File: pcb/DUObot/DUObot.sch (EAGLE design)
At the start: 1 part

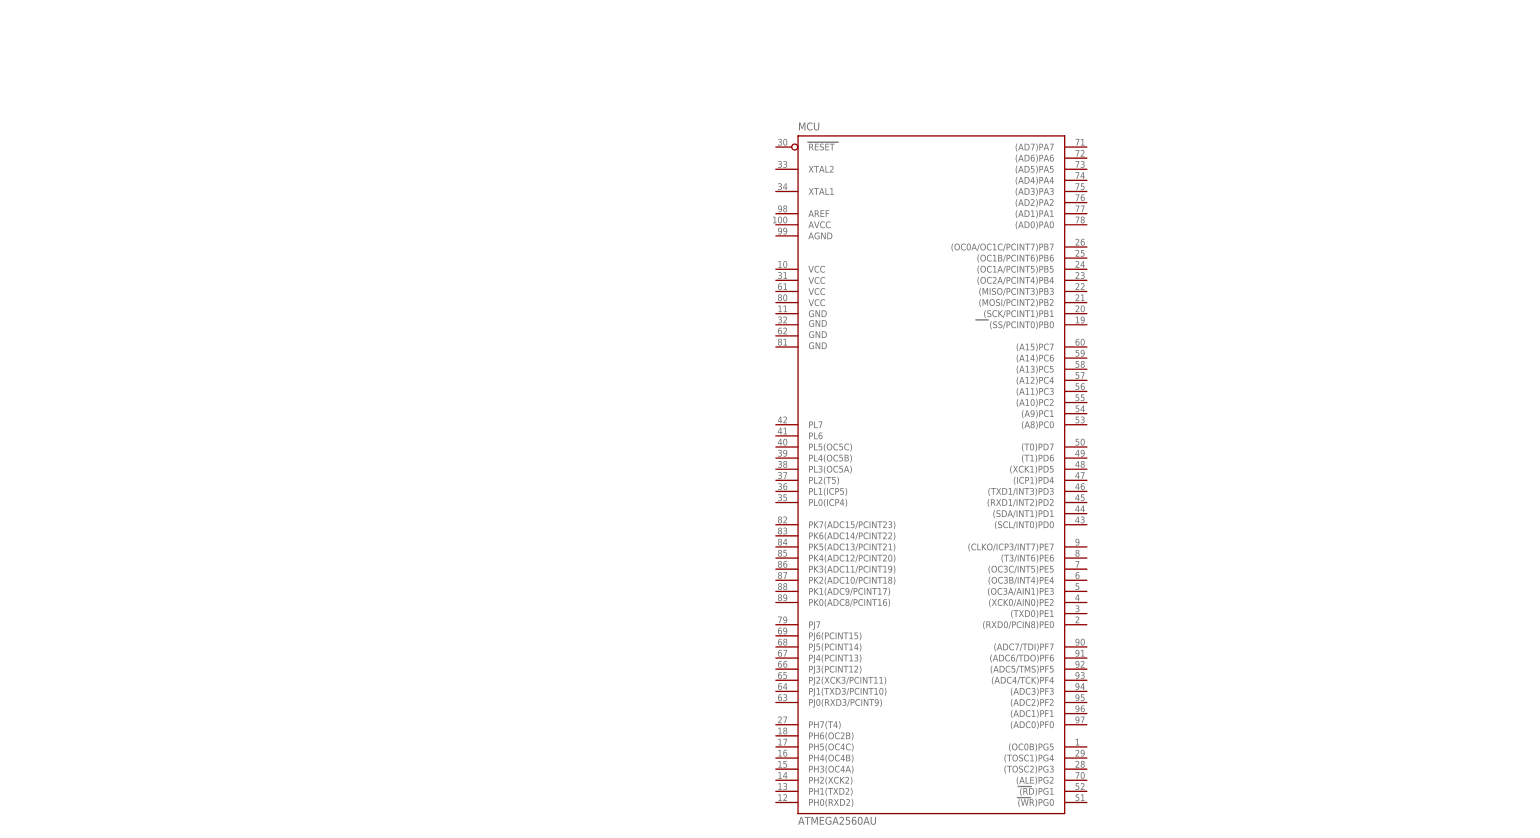
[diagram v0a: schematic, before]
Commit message: Add more components to main board. Start pcb layout
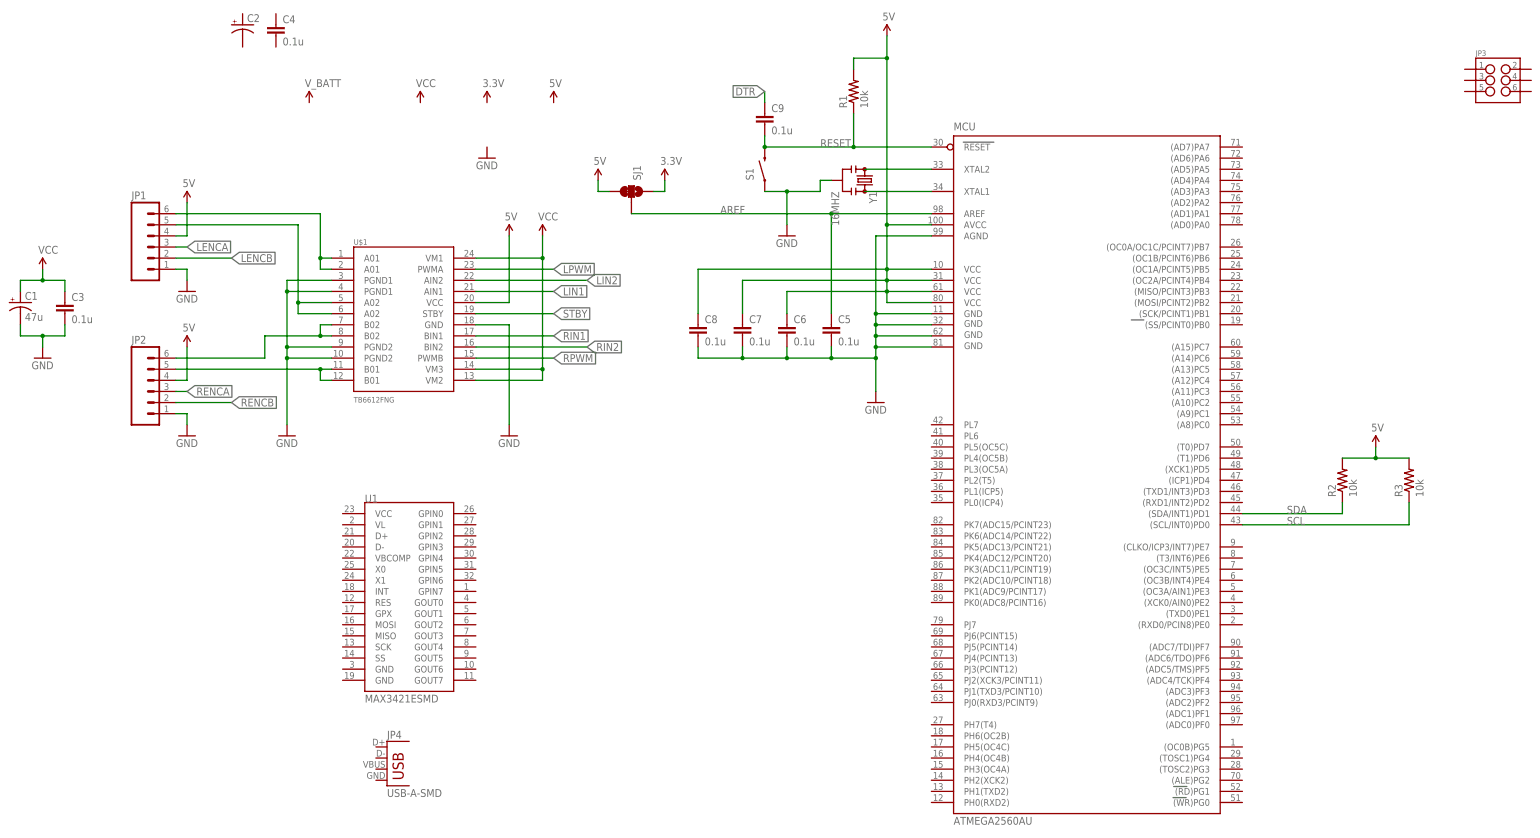
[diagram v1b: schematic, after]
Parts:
- added C1: 47u, SparkFun-Capacitors:CAP_POLD
- added C2: (no value), SparkFun-Capacitors:CAP_POLD
- added C3, C4, C5, C6, C7, C8, C9: 0.1u, SparkFun-Passives:CAP0805
- added JP1, JP2: (no value), SparkFun-Connectors:M06SMD-1MM
- added JP3: (no value), SparkFun-Connectors:M03X2SMT
- added JP4: USB-A-SMD, SparkFun-Connectors:USB-A-SMD
- added R1, R2, R3: 10k, SparkFun-Passives:RESISTOR0805-RES
- added S1: SWITCH-MOMENTARY-2SMD-4, SparkFun-Electromechanical:SWITCH-MOMENTARY-2SMD-4
- added SJ1: JUMPER-PAD-3-2OF3_NC_BY_TRACE_SMALL, SparkFun-Passives:JUMPER-PAD-3-2OF3_NC_BY_TRACE_SMALL
- added U$1: TB6612FNG, SparkFun-PowerIC:TB6612FNG
- added U1: MAX3421ESMD, SparkFun-DigitalIC:MAX3421ESMD
- added Y1: 16MHZ, SparkFun-FreqCtrl:RESONATOR16MHZ
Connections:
- new net 3.3V: SJ1.1
- new net 5V: C6.1, C7.1, C8.1, JP1.4, JP2.4, MCU.AVCC, MCU.VCC, MCU.VCC1, MCU.VCC2, MCU.VCC3, R1.2, R2.2, R3.2, SJ1.3, U$1.VCC
- new net AREF: C5.1, MCU.AREF, SJ1.2
- new net DTR: C9.1
- new net GND: C1.-, C3.2, C5.2, C6.2, C7.2, C8.2, JP1.1, JP2.1, MCU.AGND, MCU.GND, MCU.GND1, MCU.GND2, MCU.GND3, S1.1, U$1.GND, U$1.PGND1@3, U$1.PGND1@4, U$1.PGND2@10, U$1.PGND2@9, Y1.2
- new net LENCA: JP1.3
- new net LENCB: JP1.2
- new net LIN1: U$1.AIN1
- new net LIN2: U$1.AIN2
- new net LPWM: U$1.PWMA
- new net N$1: JP2.5, U$1.B01@11, U$1.B01@12
- new net N$2: JP2.6, U$1.B02@7, U$1.B02@8
- new net N$3: JP1.6, U$1.A01@1, U$1.A01@2
- new net N$4: JP1.5, U$1.A02@5, U$1.A02@6
- new net N$5: MCU.XTAL2, Y1.1
- new net N$6: MCU.XTAL1, Y1.3
- new net RENCA: JP2.3
- new net RENCB: JP2.2
- new net RESET: C9.2, MCU.RESET, R1.1, S1.2
- new net RIN1: U$1.BIN1
- new net RIN2: U$1.BIN2
- new net RPWM: U$1.PWMB
- new net SCL: MCU.(SCL/INT0)PD0, R3.1
- new net SDA: MCU.(SDA/INT1)PD1, R2.1
- new net STBY: U$1.STBY
- new net VCC: C1.+, C3.1, U$1.VM1, U$1.VM2, U$1.VM3
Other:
- moved on the sheet: MCU

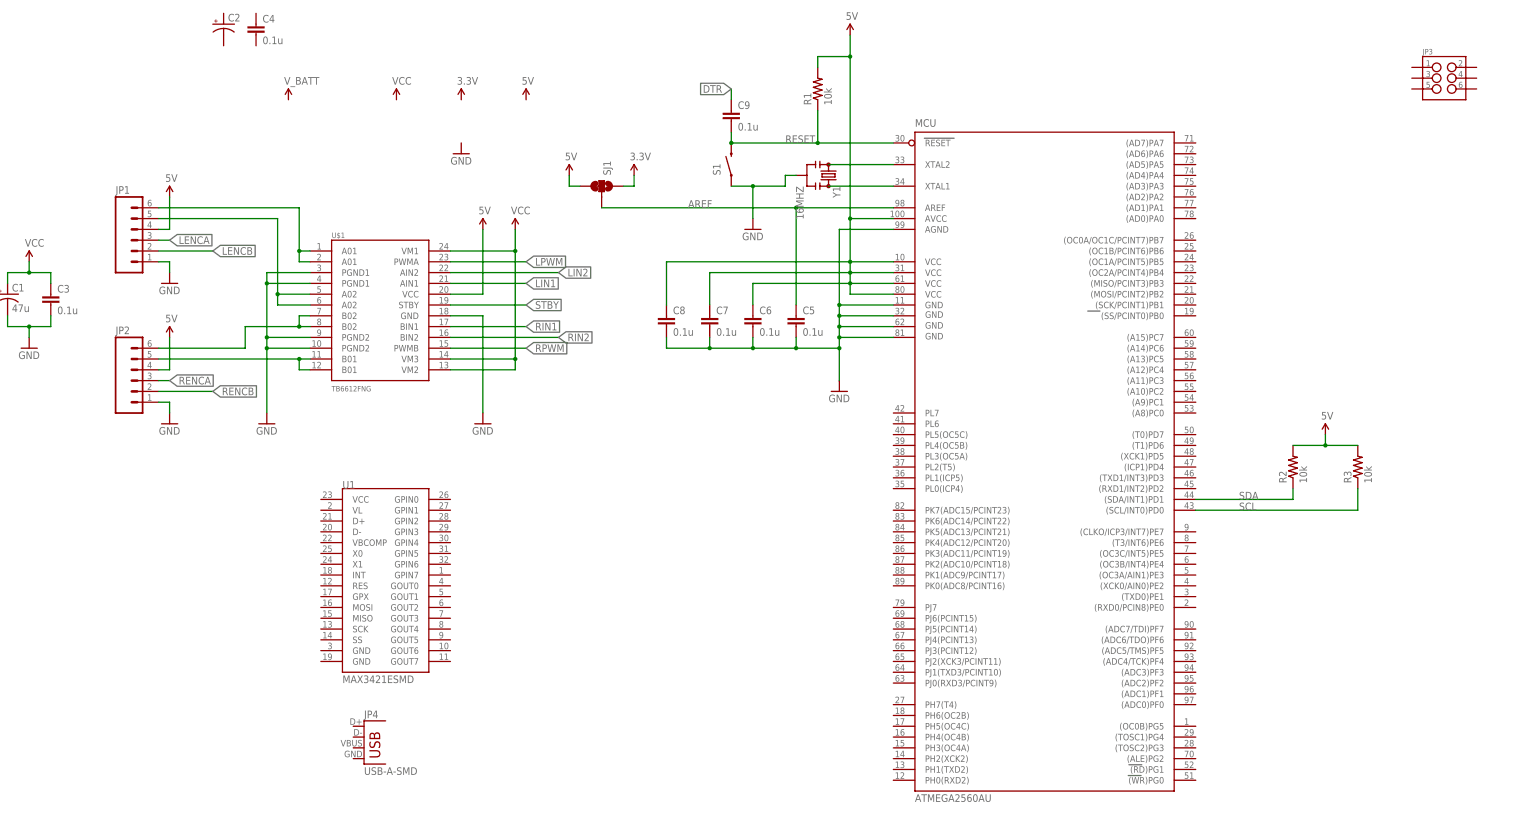
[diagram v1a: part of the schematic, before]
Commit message: Continue adding components to schematic
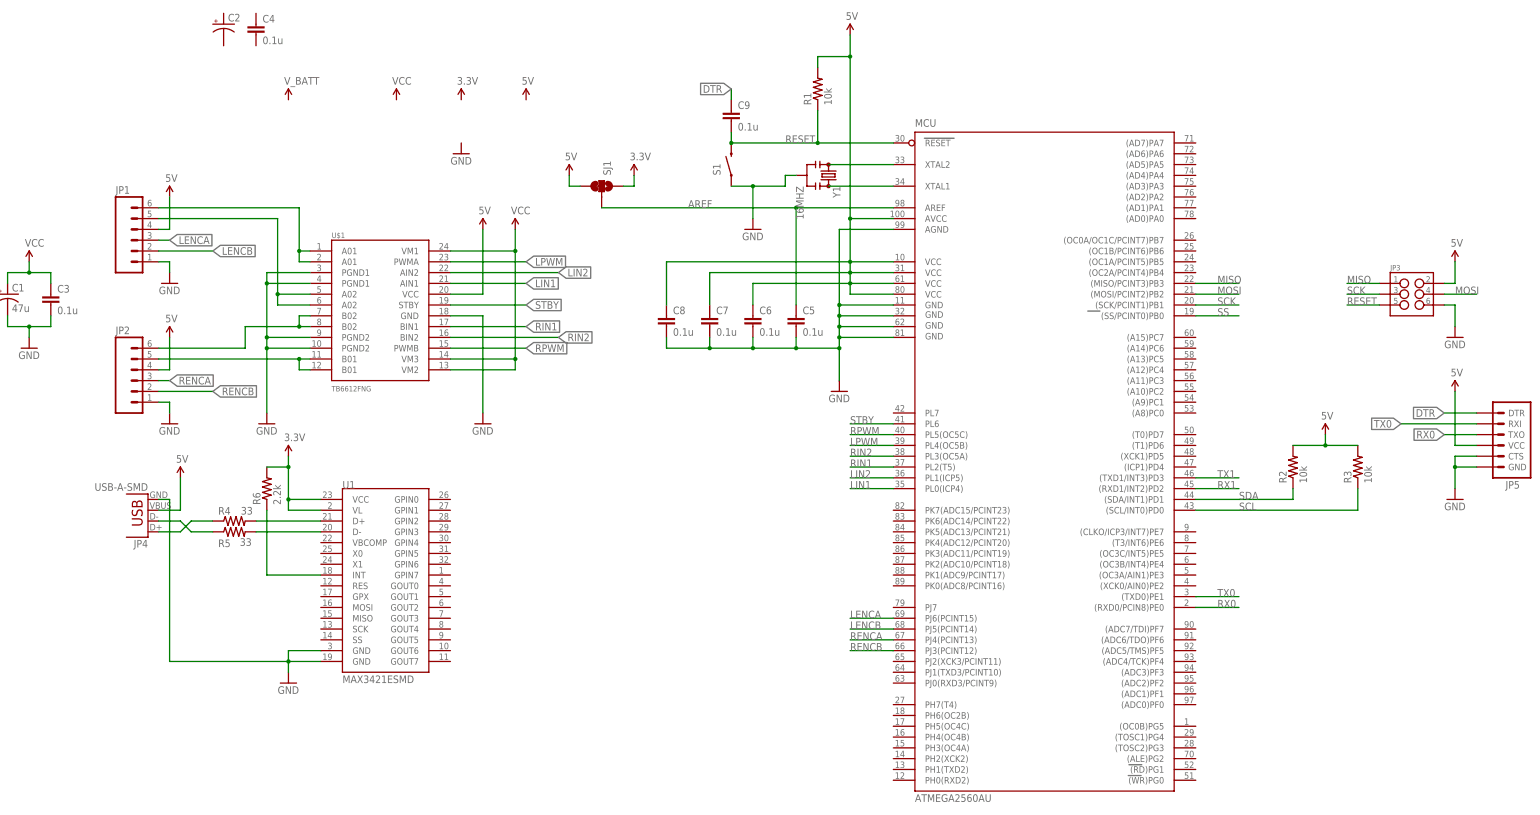
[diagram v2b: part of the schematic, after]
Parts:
- added JP5: (no value), SparkFun-Connectors:ARDUINO_SERIAL_PROGRAMPTH
- added R4, R5: 33, SparkFun-Passives:RESISTOR0805-RES
- added R6: 2.2k, SparkFun-Passives:RESISTOR0805-RES
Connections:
- new net MISO: JP3.1, MCU.(MISO/PCINT3)PB3
- new net MOSI: JP3.4, MCU.(MOSI/PCINT2)PB2
- new net N$10: JP4.D-, R5.1
- new net N$11: R6.1, U1.INT
- new net N$7: JP4.D+, R4.1
- new net N$8: R5.2, U1.D-
- new net N$9: R4.2, U1.D+
- new net RX0: JP5.TXO, MCU.(RXD0/PCIN8)PE0
- new net RX1: MCU.(RXD1/INT2)PD2
- new net SCK: JP3.3, MCU.(SCK/PCINT1)PB1
- new net SS: MCU.(SS/PCINT0)PB0
- new net TX0: JP5.RXI, MCU.(TXD0)PE1
- new net TX1: MCU.(TXD1/INT3)PD3
- net 3.3V: now also R6.2, U1.VCC, U1.VL
- net 5V: now also JP3.2, JP4.VBUS, JP5.VCC
- net DTR: now also JP5.DTR
- net GND: now also JP3.6, JP4.GND, JP5.CTS, JP5.GND, U1.GND@19, U1.GND@3
- net LENCA: now also MCU.PJ6(PCINT15)
- net LENCB: now also MCU.PJ5(PCINT14)
- net LIN1: now also MCU.PL0(ICP4)
- net LIN2: now also MCU.PL1(ICP5)
- net LPWM: now also MCU.PL4(OC5B)
- net RENCA: now also MCU.PJ4(PCINT13)
- net RENCB: now also MCU.PJ3(PCINT12)
- net RESET: now also JP3.5
- net RIN1: now also MCU.PL2(T5)
- net RIN2: now also MCU.PL3(OC5A)
- net RPWM: now also MCU.PL5(OC5C)
- net STBY: now also MCU.PL6
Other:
- moved on the sheet: JP3, JP4

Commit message: Working on power select control circuitry
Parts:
- added C10: 0.1u, SparkFun-Passives:CAP0805
- added JP6: (no value), SparkFun-Connectors:M05SMD2
- added R7: 1M, SparkFun-Passives:RESISTOR0805-RES
- JP3: value (none) -> AVR_SPI_PRG_6TESTPOINTS; device SparkFun-Connectors:M03X2SMT -> SparkFun-Connectors:AVR_SPI_PRG_6TESTPOINTS
- SJ1: value JUMPER-PAD-3-2OF3_NC_BY_TRACE_SMALL -> JUMPER-PAD-3-NOYES_SILK; device SparkFun-Passives:JUMPER-PAD-3-2OF3_NC_BY_TRACE_SMALL -> SparkFun-Passives:JUMPER-PAD-3-NOYES_SILK
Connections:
- net 3.3V: now also JP6.2
- net 5V: now also C10.1, JP6.1
- net GND: now also C10.2, JP6.3, S1.2; no longer S1.1
- net N$5: now also R7.2
- net N$6: now also R7.1
- net RESET: now also S1.1; no longer S1.2
- net SCL: now also JP6.5
- net SDA: now also JP6.4
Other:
- moved on the sheet: C1, C3, C9, JP1, JP2, R1, S1, U$1, Y1

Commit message: Main board mostly finished - needs minor changes/additions
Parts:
- removed JP1, JP2: (no value), SparkFun-Connectors:M06SMD-1MM
- removed JP3: AVR_SPI_PRG_6TESTPOINTS, SparkFun-Connectors:AVR_SPI_PRG_6TESTPOINTS
- removed JP4: USB-A-SMD, SparkFun-Connectors:USB-A-SMD
- removed JP5: (no value), SparkFun-Connectors:ARDUINO_SERIAL_PROGRAMPTH
- removed JP6: (no value), SparkFun-Connectors:M05SMD2
- added 3V3_PWR, 5V_PWR: (no value), SparkFun-LED:LED0805
- added C11, C12, C13, C15, C17: 0.1u, SparkFun-Passives:CAP0805
- added C14, C16: 10u, SparkFun-Passives:CAP_POL1206
- added C18, C19: 470p, SparkFun-Passives:CAP0805
- added D1: B340A, SparkFun-DiscreteSemi:DIODE-SCHOTTKY-B340A
- added FTDI: (no value), SparkFun-Connectors:ARDUINO_SERIAL_PROGRAMPTH
- added ICSP: AVR_SPI_PRG_6TESTPOINTS, SparkFun-Connectors:AVR_SPI_PRG_6TESTPOINTS
- added IMU: (no value), SparkFun-Connectors:M05SMD2
- added LEFT_MOTOR, RIGHT_MOTOR: (no value), SparkFun-Connectors:M06SMD-1MM
- added POWER: (no value), SparkFun-Electromechanical:SWITCH-SPDT-SMD-A
- added Q1, Q2: 200mA/50V, SparkFun-DiscreteSemi:MOSFET-NCHANNELBSS138
- added R10, R12, R13, R8, R9: (no value), SparkFun-Passives:RESISTOR0805-RES
- added R11, R14, R15, R17: 10k, SparkFun-Passives:RESISTOR0805-RES
- added R16, R18, R19: 20k, SparkFun-Passives:RESISTOR0805-RES
- added S2: SWITCH-MOMENTARY-2SMD-4, SparkFun-Electromechanical:SWITCH-MOMENTARY-2SMD-4
- added SG1: BUZZERPTH-KIT, SparkFun-Electromechanical:BUZZERPTH-KIT
- added U$2: 74AHC1G08, SparkFun-DigitalIC:74AHC1G08
- added U$3: LED-TRICOLOR, SparkFun-LED:LED-TRICOLOR
- added U$4: MCP6021T-E/OT, SparkFun-AnalogIC:MCP6021T-E/OT
- added U2: MIC5219 5V, SparkFun-PowerIC:V_REG_MIC52195V
- added U3: 3.3V/150mA, SparkFun-PowerIC:V_REG_MIC52053.3V
- added USB: USB-A-SMD, SparkFun-Connectors:USB-A-SMD
- added Y2: 12MHZ, SparkFun-FreqCtrl:RESONATOR16MHZ
- C2: value (none) -> 47u
- SJ1: value JUMPER-PAD-3-NOYES_SILK -> JUMPER-PAD-2-NOYES_SILK; device SparkFun-Passives:JUMPER-PAD-3-NOYES_SILK -> SparkFun-Passives:JUMPER-PAD-2-NOYES_SILK
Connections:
- net N$11 renamed U_INT
- new net BATT_LVL: MCU.PK7(ADC15/PCINT23), R16.1, R17.2
- new net BUZZER: MCU.(OC0B)PG5, Q1.G
- new net B_LED: MCU.(OC3A/AIN1)PE3, R9.1
- new net GPIO1: MCU.PK0(ADC8/PCINT16)
- new net GPIO2: MCU.PK1(ADC9/PCINT17)
- new net GPIO3: MCU.PK2(ADC10/PCINT18)
- new net GPIO4: MCU.PK3(ADC11/PCINT19)
- new net GPIO5: MCU.PK4(ADC12/PCINT20)
- new net GPIO6: MCU.PK5(ADC13/PCINT21)
- new net GPIO7: MCU.PK6(ADC14/PCINT22)
- new net G_LED: MCU.(OC3B/INT4)PE4, R10.1
- new net INT6: MCU.(T3/INT6)PE6
- new net INT7: MCU.(CLKO/ICP3/INT7)PE7, R11.1, S2.2
- new net N$11: R14.1, R15.2, U$4.+IN
- new net N$12: U$1.STBY, U$2.Y
- new net N$13: Q1.D, SG1.2
- new net N$14: R9.2, U$3.BLU
- new net N$15: R8.2, U$3.RED
- new net N$16: R10.2, U$3.GRN
- new net N$17: 5V_PWR.A, R12.1
- new net N$18: 3V3_PWR.A, R13.1
- new net N$19: U1.X0, Y2.1
- new net N$20: U1.X1, Y2.3
- new net N$21: C19.1, U2.BP
- new net N$22: C18.1, U3.BP
- new net N$23: U$4.V-
- new net N$24: U$4.V+
- new net N$25: D1.C, Q2.D
- new net N$27: POWER.O, R19.2
- new net N$28: POWER.S, R18.1
- new net N$29: POWER.P, Q2.G
- new net PWM1: MCU.PH3(OC4A)
- new net PWM2: MCU.PH4(OC4B)
- new net PWM3: MCU.PH5(OC4C)
- new net R_LED: MCU.(OC3C/INT5)PE5, R8.1
- new net U_MISO: U1.MISO
- new net U_MOSI: U1.MOSI
- new net U_RES: U1.RES
- new net U_SCK: U1.SCK
- new net U_SS: U1.SS
- new net V_BATT: D1.A, R18.2
- new net V_COMP: U$2.A, U$4.OUT
- net 3.3V: now also C11.1, C12.1, C14.+, C17.1, IMU.2, R13.2, SJ1.2, U$4.-IN, U3.OUT; no longer JP6.2, SJ1.1
- net 5V: now also C13.1, C15.1, C16.+, FTDI.VCC, ICSP.2, IMU.1, LEFT_MOTOR.4, R11.2, R12.2, RIGHT_MOTOR.4, SG1.1, U$2.VCC, U$3.A, U2.OUT, U3.EN, U3.IN, USB.VBUS; no longer JP1.4, JP2.4, JP3.2, JP4.VBUS, JP5.VCC, JP6.1, SJ1.3
- net AREF: now also SJ1.1; no longer SJ1.2
- net DTR: now also FTDI.DTR; no longer JP5.DTR
- net GND: now also 3V3_PWR.C, 5V_PWR.C, C11.2, C12.2, C13.2, C14.-, C15.2, C16.-, C17.2, C18.2, C19.2, C2.-, C4.2, FTDI.CTS, FTDI.GND, ICSP.6, IMU.3, LEFT_MOTOR.1, Q1.S, R15.1, R17.1, R19.1, RIGHT_MOTOR.1, S2.1, U$2.GND, U2.GND, U3.GND, USB.GND, Y2.2; no longer JP1.1, JP2.1, JP3.6, JP4.GND, JP5.CTS, JP5.GND, JP6.3
- net LENCA: now also LEFT_MOTOR.3; no longer JP1.3
- net LENCB: now also LEFT_MOTOR.2; no longer JP1.2
- net MISO: now also ICSP.1; no longer JP3.1
- net MOSI: now also ICSP.4; no longer JP3.4
- net N$1: now also RIGHT_MOTOR.5; no longer JP2.5
- net N$10: now also USB.D-; no longer JP4.D-
- net N$2: now also RIGHT_MOTOR.6; no longer JP2.6
- net N$3: now also LEFT_MOTOR.6; no longer JP1.6
- net N$4: now also LEFT_MOTOR.5; no longer JP1.5
- net N$7: now also USB.D+; no longer JP4.D+
- net RENCA: now also RIGHT_MOTOR.3; no longer JP2.3
- net RENCB: now also RIGHT_MOTOR.2; no longer JP2.2
- net RESET: now also ICSP.5; no longer JP3.5
- net RX0: now also FTDI.TXO; no longer JP5.TXO
- net SCK: now also ICSP.3; no longer JP3.3
- net SCL: no longer JP6.5, R3.1
- net SDA: no longer JP6.4, R2.1
- net STBY: now also U$2.B; no longer U$1.STBY
- net TX0: now also FTDI.RXI; no longer JP5.RXI
- net VCC: now also C2.+, C4.1, Q2.S, R14.2, R16.2, U2.EN, U2.IN
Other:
- note added: "ATmega2560"
- note added: "Breakout"
- note added: "I2C"
- note added: "ICSP"
- note added: "Motor Driver"
- note added: "Power Supply"
- note added: "Serial/FTDI"
- note added: "Status"
- note added: "USB Host"
- moved on the sheet: C1, C10, C2, C3, C4, C5, C6, C7, C8, C9, MCU, R1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

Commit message: Change individual pull-up resistors to arrays
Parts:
- removed R2, R3: 10k, SparkFun-Passives:RESISTOR0805-RES
- added R22, R23, R24, R34: (no value), SparkFun-Resistors:RESISTOR-ARRAY0603-ARV
- added U$5, U$6, U$7, U$8: MOSFET, SparkFun-DiscreteSemi:MOSFET
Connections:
- new net N$32: IMU.4, R24R.1, U$5G$1.S
- new net N$33: IMU.5, R24D.1, U$5G$2.S
- new net N$37: R23B.1, U$6G$1.D
- new net N$38: R23A.1, U$6G$2.D
- net 3.3V: now also R22A.2, R22B.2, R22D.2, R22R.2, R23D.2, R23R.2, R24D.2, R24R.2, U$5G$1.G, U$5G$2.G, U$6G$1.G, U$6G$2.G, U$7G$1.G, U$7G$2.G, U$8G$1.G, U$8G$2.G
- net 5V: now also R23A.2, R23B.2, R24A.2, R24B.2, R34A.2, R34B.2, R34D.2, R34R.2; no longer R2.2, R3.2
- net MISO: now also R34B.1, U$7G$2.D
- net MOSI: now also R34A.1, U$7G$1.D
- net SCK: now also R34D.1, U$8G$1.D
- net SCL: now also R24A.1, U$5G$2.D
- net SDA: now also R24B.1, U$5G$1.D
- net SS: now also R34R.1, U$8G$2.D
- net U_INT: now also R23D.1, U$6G$1.S
- net U_MISO: now also R22R.1, U$7G$2.S
- net U_MOSI: now also R22D.1, U$7G$1.S
- net U_RES: now also R23R.1, U$6G$2.S
- net U_SCK: now also R22B.1, U$8G$1.S
- net U_SS: now also R22A.1, U$8G$2.S
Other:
- moved on the sheet: C11, C12, C13, R4, R5, R6, U1, USB, Y2
